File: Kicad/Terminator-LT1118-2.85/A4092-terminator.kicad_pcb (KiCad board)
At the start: 2 copper layers, 72.3 x 17.6 mm, 10 parts, among them J1 Conn_02x25_Odd_Even, U1 LT1118-2.85

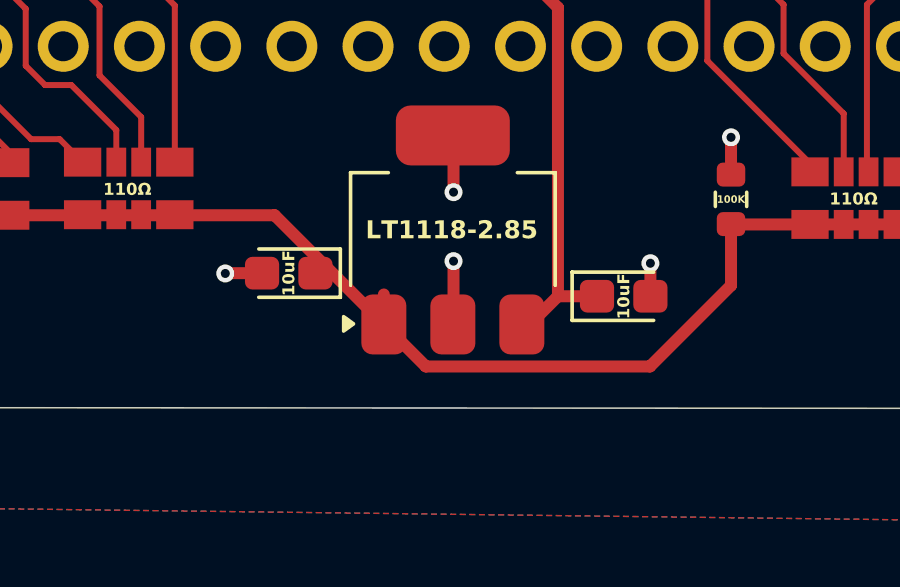
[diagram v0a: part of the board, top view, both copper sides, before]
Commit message: Update LT1118-2.85 based terminator
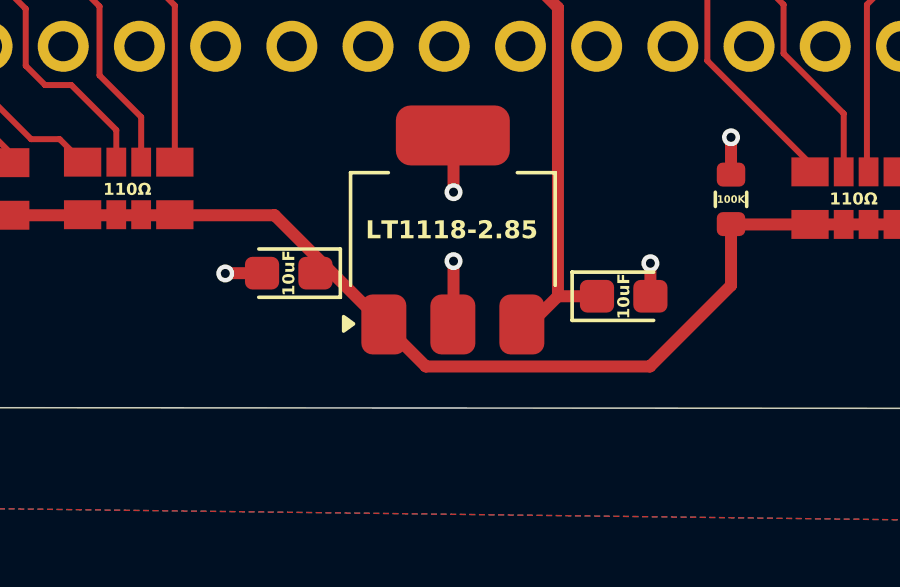
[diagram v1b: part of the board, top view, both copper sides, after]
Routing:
- net 2V85: track 49.0 -> 47.5 mm
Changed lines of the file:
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@@
 		(tags "resistor")
 		(property "Reference" "R3"
-			(at -2.56 0.06 180)
+			(at -2.56 0.06 0)
 			(layer "F.SilkS")
 			(hide yes)
@@
 			)
 		)
-		(property "LCSC Part #" ""
+		(property "LCSC Part #" "C25803"
 			(at 0 0 270)
 			(unlocked yes)
@@
 	)
 	(gr_text "Rev A"
-		(at 157.42 39.81 90)
+		(at 157.07 40.34 90)
 		(layer "F.Mask")
 		(effects
 			(font
-				(size 1 1)
-				(thickness 0.1)
+				(size 1.25 1.25)
+				(thickness 0.25)
+				(bold yes)
 			)
 			(justify left bottom)
@@
 	)
 	(segment
-		(start 122.2575 48.24)
-		(end 122.4375 48.42)
-		(width 0.4)
-		(layer "F.Cu")
-		(net 1)
-	)
-	(segment
 		(start 123.461 47.299)
 		(end 122.28 48.48)
@@
 	)
 	(segment
-		(start 117.6575 48.24)
-		(end 117.6575 47.24)
-		(width 0.4)
-		(layer "F.Cu")
-		(net 3)
-	)
-	(segment
 		(start 144.28431 44.9063)
 		(end 144.30801 44.8826)
@@
 		(width 0.4)
 		(layer "F.Cu")
-		(net 3)
-	)
-	(segment
-		(start 117.2875 48.61)
-		(end 117.6575 48.24)
-		(width 0.4)
-		(layer "F.Cu")
